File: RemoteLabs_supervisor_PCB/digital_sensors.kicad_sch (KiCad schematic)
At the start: 8 parts, among them J23 limit_switch_A, J24 limit_switch_B, J25 Optical Encoder

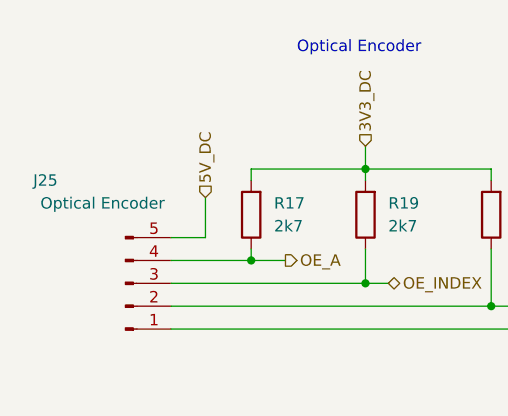
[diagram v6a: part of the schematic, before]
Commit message: Updated PCB for V1.1 see CHANGELOG
Test software refinement
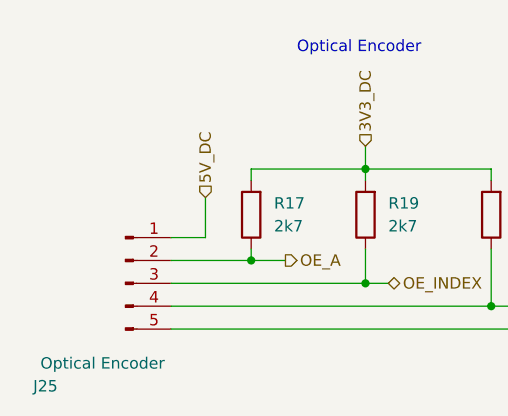
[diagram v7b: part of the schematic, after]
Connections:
- net 5V_DC: now also J25.1 (Pin_1); no longer J25.5 (Pin_5)
- net GND_D: now also J25.5 (Pin_5); no longer J25.1 (Pin_1)
- net OE_A: now also J25.2 (Pin_2); no longer J25.4 (Pin_4)
- net OE_B: now also J25.4 (Pin_4); no longer J25.2 (Pin_2)
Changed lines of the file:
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@@
     (pin "2")
   )
-  (symbol (lib_id "000_Pin_Headers_Immo:Molex_5pin_2.54mm_M") (at 87.63 106.68 0) (mirror x) (unit 1)
+  (symbol (lib_id "000_Pin_Headers_Immo:Molex_5pin_2.54mm_M") (at 87.63 106.68 0) (unit 1)
     (in_bom yes) (on_board yes)
-    (property "Reference" "J25" (id 0) (at 78.74 95.25 0))
-    (property "Value" "Optical Encoder" (id 1) (at 85.09 97.79 0))
-    (property "Footprint" "Connector_Molex:Molex_KK-254_AE-6410-05A_1x05_P2.54mm_Vertical" (id 2) (at 89.535 96.52 0)
+    (property "Reference" "J25" (id 0) (at 78.74 118.11 0))
+    (property "Value" "Optical Encoder" (id 1) (at 85.09 115.57 0))
+    (property "Footprint" "Connector_Molex:Molex_KK-254_AE-6410-05A_1x05_P2.54mm_Vertical" (id 2) (at 89.535 116.84 0)
       (effects (font (size 1.27 1.27)) hide)
     )
